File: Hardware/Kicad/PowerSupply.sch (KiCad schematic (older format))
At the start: 7 parts, among them IC301 LM1086-5.0, IC302 LM1086-3.3, P301 POWER IN, P302 3.3V PWR 5V

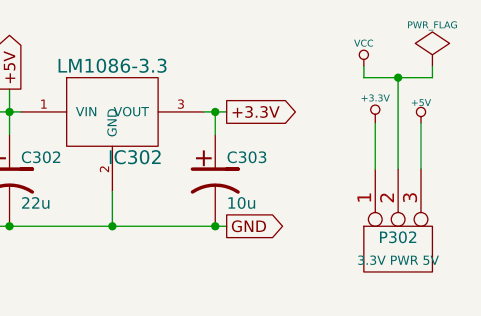
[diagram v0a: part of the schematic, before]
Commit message: Schematic updates
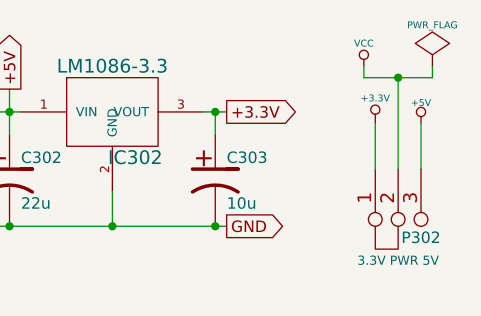
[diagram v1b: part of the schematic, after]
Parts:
- removed P302: 3.3V PWR 5V, ~, symbol CONN_3
- added P302: 3.3V PWR 5V, ~, symbol 00JG-JUMPER-SHORTED
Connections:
- net +3.3V: now also P302.1 (P1)
- net +5V: now also P302.3 (P3)
- net VCC: now also P302.2 (PM)
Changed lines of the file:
@@
 Sheet 3 7
 Title "Propeddle"
-Date "8 apr 2014"
+Date "18 apr 2014"
 Rev "10"
 Comp "(C) 2014 Jac Goudsmit"
@@
 +3.3V
 $Comp
-L CONN_3 P302
-U 1 1 5345FAE2
-P 7600 4150
-F 0 "P302" V 7550 4150 50  0000 C CNN
-F 1 "3.3V PWR 5V" V 7650 4150 40  0000 C CNN
-F 2 "~" H 7600 4150 60  0000 C CNN
-F 3 "~" H 7600 4150 60  0000 C CNN
-	1    7600 4150
-	0    -1   1    0
-$EndComp
-$Comp
 L +5V #PWR021
 U 1 1 53460456
@@
 Wire Wire Line
 	7450 3350 7450 3400
+$Comp
+L 00JG-JUMPER-SHORTED P302
+U 1 1 5347D614
+P 7600 4150
+F 0 "P302" V 7550 4050 50  0000 C CNN
+F 1 "3.3V PWR 5V" V 7650 4150 40  0000 C CNN
+F 2 "~" H 7600 4150 60  0000 C CNN
+F 3 "~" H 7600 4150 60  0000 C CNN
+	1    7600 4150
+	0    -1   1    0
+$EndComp
 $EndSCHEMATC

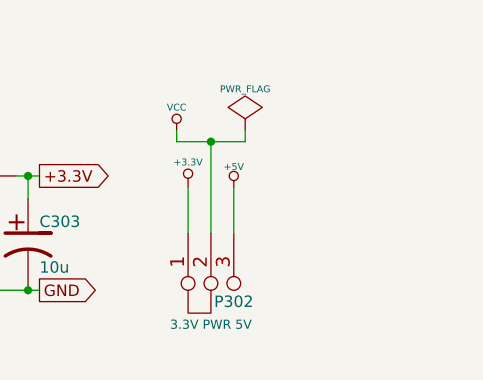
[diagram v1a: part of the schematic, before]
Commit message: Schematic Rev. 11
Added LEDs; some minor other modifications
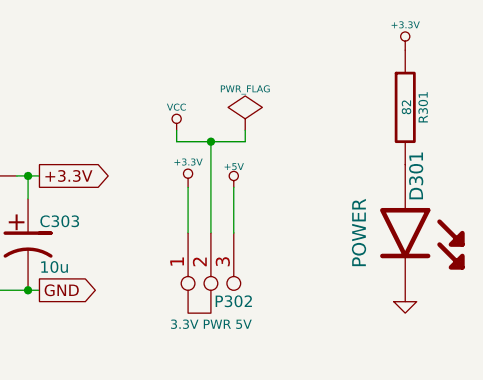
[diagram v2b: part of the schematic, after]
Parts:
- added D301: POWER, symbol LED
- added R301: 82, ~, symbol R
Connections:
- net +3.3V: now also R301.1
- net GND: now also D301.K
- new net: D301.A, R301.2
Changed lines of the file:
@@
 Title "Propeddle"
 Date "18 apr 2014"
-Rev "10"
+Rev "11"
 Comp "(C) 2014 Jac Goudsmit"
 Comment1 "Software-Defined 6502 Computer"
@@
 	0    -1   1    0
 $EndComp
+$Comp
+L LED D301
+U 1 1 53519983
+P 8450 3800
+F 0 "D301" H 8200 3850 60  0000 C CNN
+F 1 "POWER" H 8450 3600 60  0000 C CNN
+F 2 "" H 8450 3800 60  0000 C CNN
+F 3 "" H 8450 3800 60  0000 C CNN
+	1    8450 3800
+	0    1    1    0
+$EndComp
+$Comp
+L GND #PWR025
+U 1 1 53519992
+P 8450 4100
+F 0 "#PWR025" H 8450 4100 30  0001 C CNN
+F 1 "GND" H 8450 4030 30  0001 C CNN
+F 2 "" H 8450 4100 60  0000 C CNN
+F 3 "" H 8450 4100 60  0000 C CNN
+	1    8450 4100
+	1    0    0    -1
+$EndComp
+$Comp
+L R R301
+U 1 1 535199A1
+P 8450 3250
+F 0 "R301" V 8530 3250 40  0000 C CNN
+F 1 "82" V 8457 3251 40  0000 C CNN
+F 2 "~" V 8380 3250 30  0000 C CNN
+F 3 "~" H 8450 3250 30  0000 C CNN
+	1    8450 3250
+	1    0    0    -1
+$EndComp
+$Comp
+L +3.3V #PWR026
+U 1 1 535199B0
+P 8450 3000
+F 0 "#PWR026" H 8450 2960 30  0001 C CNN
+F 1 "+3.3V" H 8450 3110 30  0000 C CNN
+F 2 "" H 8450 3000 60  0000 C CNN
+F 3 "" H 8450 3000 60  0000 C CNN
+	1    8450 3000
+	1    0    0    -1
+$EndComp
 $EndSCHEMATC
